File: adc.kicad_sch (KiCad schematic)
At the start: 45 parts, among them J10 Conn_01x02_Pin, J11 Conn_01x02_Pin, J12 Conn_01x02_Pin, J14 Conn_01x02_Pin, J4 Conn_01x03_Pin, J5 Conn_01x03_Pin, J8 Conn_01x03_Pin, J9 Conn_01x03_Pin, U9 LTC2299xUP

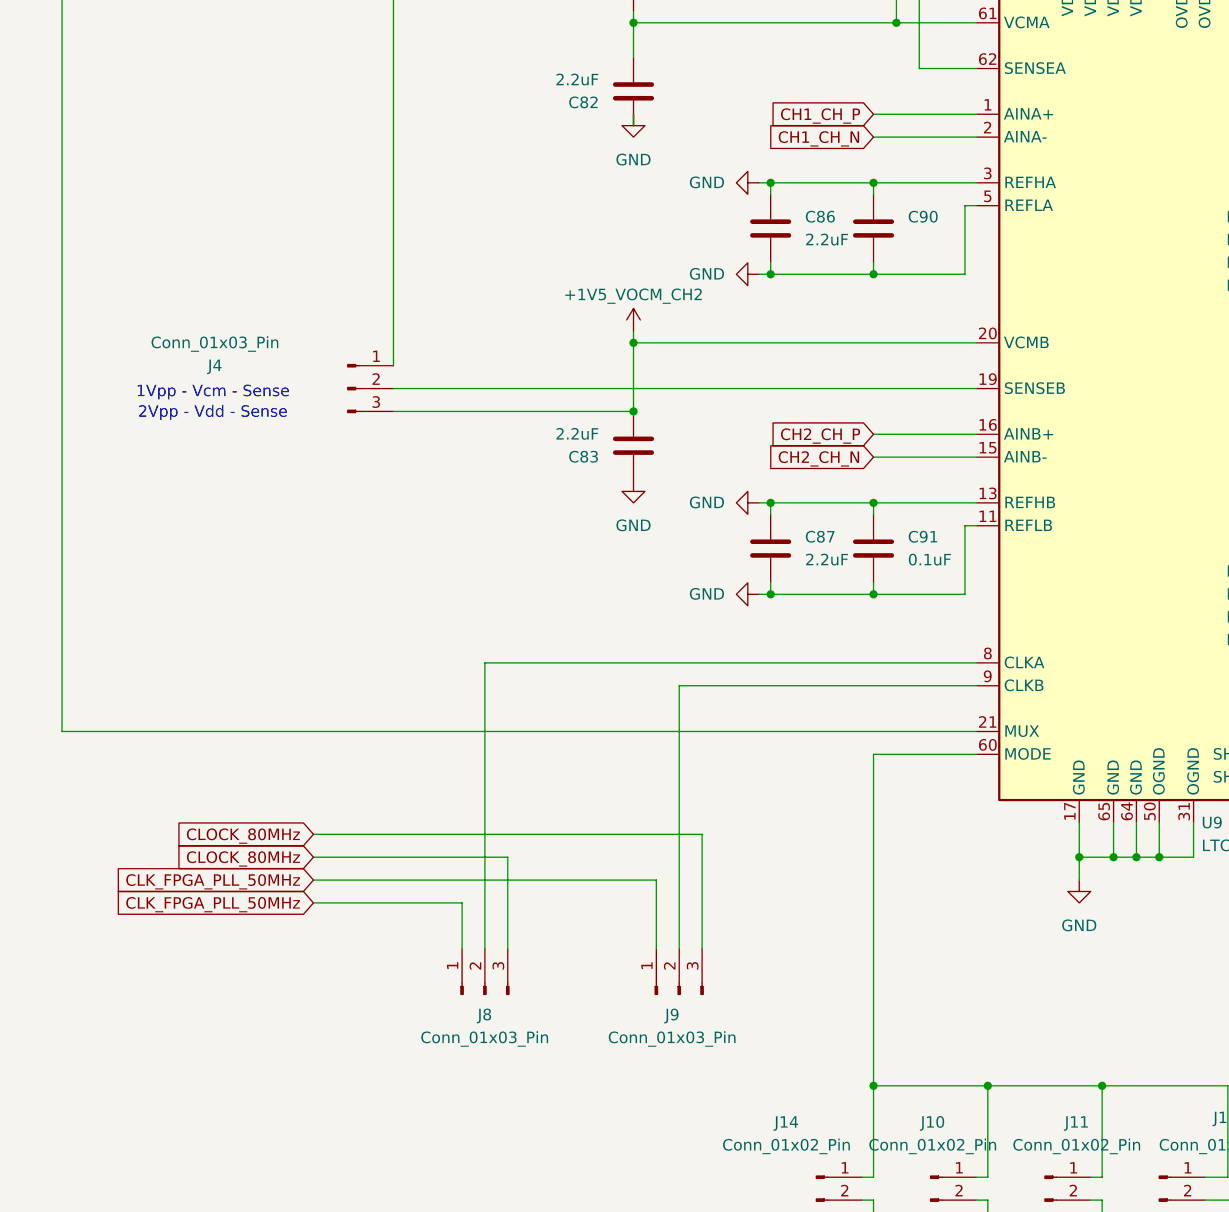
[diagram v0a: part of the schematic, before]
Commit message: Add LDO's
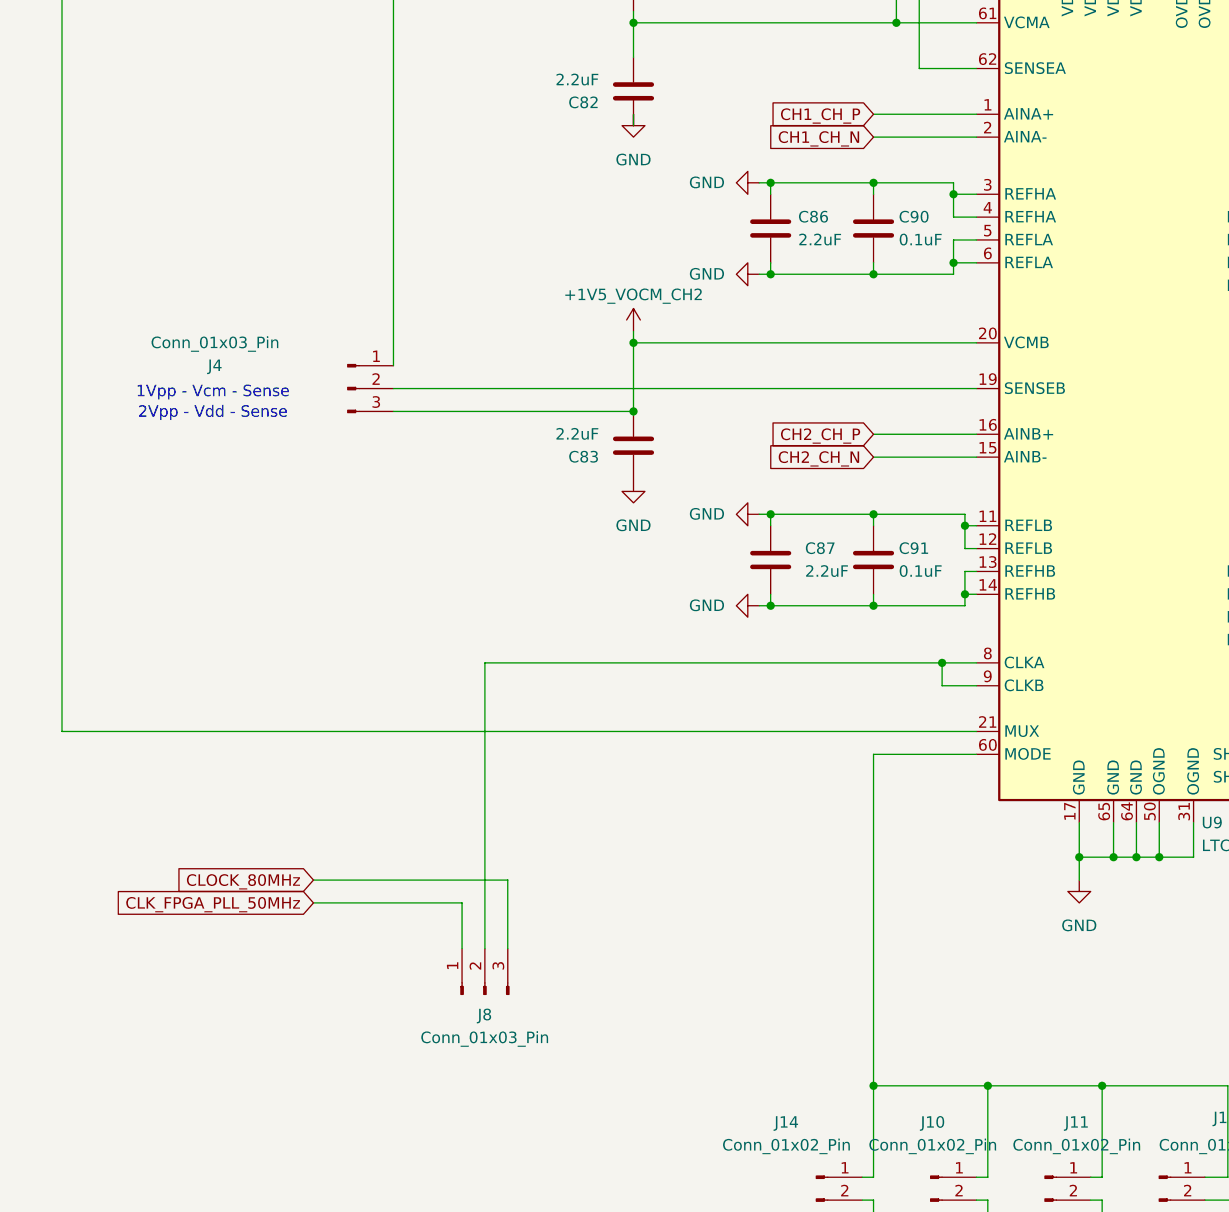
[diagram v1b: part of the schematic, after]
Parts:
- removed J9: Conn_01x03_Pin, Connector_PinHeader_2.54mm:PinHeader_1x03_P2.54mm_Vertical, symbol Connector:Conn_01x03_Pin
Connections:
- net at J8.2 (Pin_2), U9.8 (CLKA): now also U9.9 (CLKB)
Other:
- moved on the sheet: C87, C91

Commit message: Do most of the PCB
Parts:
- J4, J5: footprint TerminalBlock:TerminalBlock_MaiXu_MX126-5.0-03P_1x03_P5.00mm -> Connector_PinHeader_2.54mm:PinHeader_1x03_P2.54mm_Vertical
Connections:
- net GND: now also R68.2, R70.2
- net at R69.2, R70.1: now also J10.2 (Pin_2)
- net at J11.2 (Pin_2): now also R67.2, R68.1; no longer R68.2
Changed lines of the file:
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@@
 	)
 	(junction
+		(at 266.7 245.11)
+		(diameter 0)
+		(color 0 0 0 0)
+	)
+	(junction
 		(at 203.2 256.54)
 		(diameter 0)
@@
 	)
 	(junction
+		(at 279.4 245.11)
+		(diameter 0)
+		(color 0 0 0 0)
+	)
+	(junction
 		(at 232.41 231.14)
 		(diameter 0)
@@
 	(wire
 		(pts
-			(xy 266.7 243.84) (xy 266.7 247.65)
+			(xy 266.7 243.84) (xy 266.7 245.11)
 		)
 		(stroke
@@
 		)
 	)
+	(wire
+		(pts
+			(xy 274.32 276.86) (xy 274.32 245.11)
+		)
+		(stroke
+			(width 0)
+			(type default)
+		)
+	)
 	(bus
 		(pts
@@
 	(wire
 		(pts
+			(xy 279.4 255.27) (xy 279.4 257.81)
+		)
+		(stroke
+			(width 0)
+			(type default)
+		)
+	)
+	(wire
+		(pts
 			(xy 173.99 86.36) (xy 173.99 83.82)
 		)
@@
 		)
 	)
+	(wire
+		(pts
+			(xy 257.81 245.11) (xy 266.7 245.11)
+		)
+		(stroke
+			(width 0)
+			(type default)
+		)
+	)
 	(bus
 		(pts
@@
 	(wire
 		(pts
+			(xy 279.4 245.11) (xy 279.4 247.65)
+		)
+		(stroke
+			(width 0)
+			(type default)
+		)
+	)
+	(wire
+		(pts
 			(xy 191.77 166.37) (xy 190.5 166.37)
 		)
@@
 	(wire
 		(pts
+			(xy 266.7 257.81) (xy 266.7 255.27)
+		)
+		(stroke
+			(width 0)
+			(type default)
+		)
+	)
+	(wire
+		(pts
 			(xy 132.08 57.15) (xy 139.7 57.15)
 		)
@@
 	(wire
 		(pts
+			(xy 266.7 245.11) (xy 266.7 247.65)
+		)
+		(stroke
+			(width 0)
+			(type default)
+		)
+	)
+	(wire
+		(pts
 			(xy 203.2 156.21) (xy 203.2 157.48)
 		)
@@
 	(wire
 		(pts
+			(xy 274.32 245.11) (xy 279.4 245.11)
+		)
+		(stroke
+			(width 0)
+			(type default)
+		)
+	)
+	(wire
+		(pts
 			(xy 215.9 276.86) (xy 215.9 269.24)
 		)
@@
 	(wire
 		(pts
+			(xy 257.81 273.05) (xy 257.81 245.11)
+		)
+		(stroke
+			(width 0)
+			(type default)
+		)
+	)
+	(wire
+		(pts
 			(xy 212.09 160.02) (xy 212.09 157.48)
 		)
@@
 	(wire
 		(pts
-			(xy 266.7 273.05) (xy 228.6 273.05)
-		)
-		(stroke
-			(width 0)
-			(type default)
-		)
-	)
-	(wire
-		(pts
 			(xy 185.42 93.98) (xy 185.42 97.79)
 		)
@@
 	(wire
 		(pts
-			(xy 266.7 255.27) (xy 266.7 273.05)
-		)
-		(stroke
-			(width 0)
-			(type default)
-		)
-	)
-	(wire
-		(pts
 			(xy 176.53 173.99) (xy 176.53 172.72)
 		)
@@
 	(wire
 		(pts
-			(xy 279.4 243.84) (xy 279.4 247.65)
+			(xy 279.4 243.84) (xy 279.4 245.11)
 		)
 		(stroke
@@
 	(wire
 		(pts
-			(xy 279.4 255.27) (xy 279.4 276.86)
-		)
-		(stroke
-			(width 0)
-			(type default)
-		)
-	)
-	(wire
-		(pts
 			(xy 203.2 186.69) (xy 214.63 186.69)
 		)
@@
 	(wire
 		(pts
-			(xy 279.4 276.86) (xy 215.9 276.86)
+			(xy 271.78 57.15) (xy 279.4 57.15)
 		)
 		(stroke
@@
 	(wire
 		(pts
-			(xy 271.78 57.15) (xy 279.4 57.15)
+			(xy 224.79 106.68) (xy 224.79 128.27)
 		)
 		(stroke
@@
 	(wire
 		(pts
-			(xy 224.79 106.68) (xy 224.79 128.27)
+			(xy 173.99 59.69) (xy 173.99 57.15)
 		)
 		(stroke
@@
 		)
 	)
-	(wire
+	(bus
 		(pts
-			(xy 173.99 59.69) (xy 173.99 57.15)
+			(xy 280.67 181.61) (xy 280.67 184.15)
 		)
 		(stroke
@@
 		)
 	)
-	(bus
+	(wire
 		(pts
-			(xy 280.67 181.61) (xy 280.67 184.15)
+			(xy 228.6 273.05) (xy 257.81 273.05)
 		)
 		(stroke
@@
 	(wire
 		(pts
+			(xy 215.9 276.86) (xy 274.32 276.86)
+		)
+		(stroke
+			(width 0)
+			(type default)
+		)
+	)
+	(wire
+		(pts
 			(xy 229.87 130.81) (xy 229.87 128.27)
 		)
@@
 			)
 		)
-		(property "Footprint" "TerminalBlock:TerminalBlock_MaiXu_MX126-5.0-03P_1x03_P5.00mm"
+		(property "Footprint" "Connector_PinHeader_2.54mm:PinHeader_1x03_P2.54mm_Vertical"
 			(at 208.28 123.19 0)
 			(effects
@@
 	)
 	(symbol
+		(lib_id "power:GND")
+		(at 266.7 257.81 0)
+		(unit 1)
+		(exclude_from_sim no)
+		(in_bom yes)
+		(on_board yes)
+		(dnp no)
+		(fields_autoplaced yes)
+		(property "Reference" "#PWR0275"
+			(at 266.7 264.16 0)
+			(effects
+				(font
+					(size 1.27 1.27)
+				)
+				(hide yes)
+			)
+		)
+		(property "Value" "GND"
+			(at 266.7 262.89 0)
+			(effects
+				(font
+					(size 1.27 1.27)
+				)
+			)
+		)
+		(property "Footprint" ""
+			(at 266.7 257.81 0)
+			(effects
+				(font
+					(size 1.27 1.27)
+				)
+				(hide yes)
+			)
+		)
+		(property "Datasheet" ""
+			(at 266.7 257.81 0)
+			(effects
+				(font
+					(size 1.27 1.27)
+				)
+				(hide yes)
+			)
+		)
+		(property "Description" "Power symbol creates a global label with name \"GND\" , ground"
+			(at 266.7 257.81 0)
+			(effects
+				(font
+					(size 1.27 1.27)
+				)
+				(hide yes)
+			)
+		)
+		(pin "1"
+		)
+		(instances
+			(project "DigitalOsciloscope"
+				(path "/553deb7b-4100-40fe-99d2-0c7b4b56aad2/800cc051-5da0-4b0f-90b7-cfba3f489ea8"
+					(reference "#PWR0275")
+					(unit 1)
+				)
+			)
+		)
+	)
+	(symbol
 		(lib_id "Connector:Conn_01x02_Pin")
 		(at 209.55 266.7 0)
@@
 			)
 		)
-		(property "Footprint" "TerminalBlock:TerminalBlock_MaiXu_MX126-5.0-03P_1x03_P5.00mm"
+		(property "Footprint" "Connector_PinHeader_2.54mm:PinHeader_1x03_P2.54mm_Vertical"
 			(at 144.78 179.07 0)
 			(effects
@@
 					(unit 1)
 				)
+			)
+		)
+	)
+	(symbol
+		(lib_id "power:GND")
+		(at 279.4 257.81 0)
+		(unit 1)
+		(exclude_from_sim no)
+		(in_bom yes)
+		(on_board yes)
+		(dnp no)
+		(fields_autoplaced yes)
+		(property "Reference" "#PWR0278"
+			(at 279.4 264.16 0)
+			(effects
+				(font
+					(size 1.27 1.27)
+				)
+				(hide yes)
+			)
+		)
+		(property "Value" "GND"
+			(at 279.4 262.89 0)
+			(effects
+				(font
+					(size 1.27 1.27)
+				)
+			)
+		)
+		(property "Footprint" ""
+			(at 279.4 257.81 0)
+			(effects
+				(font
+					(size 1.27 1.27)
+				)
+				(hide yes)
+			)
+		)
+		(property "Datasheet" ""
+			(at 279.4 257.81 0)
+			(effects
+				(font
+					(size 1.27 1.27)
+				)
+				(hide yes)
+			)
+		)
+		(property "Description" "Power symbol creates a global label with name \"GND\" , ground"
+			(at 279.4 257.81 0)
+			(effects
+				(font
+					(size 1.27 1.27)
+				)
+				(hide yes)
+			)
+		)
+		(pin "1"
+		)
+		(instances
+			(project "DigitalOsciloscope"
+				(path "/553deb7b-4100-40fe-99d2-0c7b4b56aad2/800cc051-5da0-4b0f-90b7-cfba3f489ea8"
+					(reference "#PWR0278")
+					(unit 1)
+				)

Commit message: Place all componenets
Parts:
- renumbered C98 to C100, C99 to C101, C76 to C78, C77 to C79, C78 to C80, C79 to C81, C80 to C82, C81 to C83, C82 to C84, C83 to C85, C84 to C86, C85 to C87, C86 to C88, C87 to C89, C88 to C90, C89 to C91, C90 to C92, C91 to C93, C92 to C94, C93 to C95, C94 to C96, C95 to C97, C96 to C98, C97 to C99, J12 to J10, J8 to J5, J14 to J6, J5 to J7, J10 to J8, J11 to J9, R67 to R54, R68 to R55, R69 to R56, R70 to R57

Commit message: Finish channel 1 rework
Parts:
- renumbered C101 to C100, C78 to C77, C79 to C78, C80 to C79, C81 to C80, C82 to C81, C83 to C82, C84 to C83, C85 to C84, C86 to C85, C87 to C86, C88 to C87, C89 to C88, C90 to C89, C91 to C90, C92 to C91, C93 to C92, C94 to C93, C95 to C94, C96 to C95, C97 to C96, C98 to C97, C99 to C98, C100 to C99

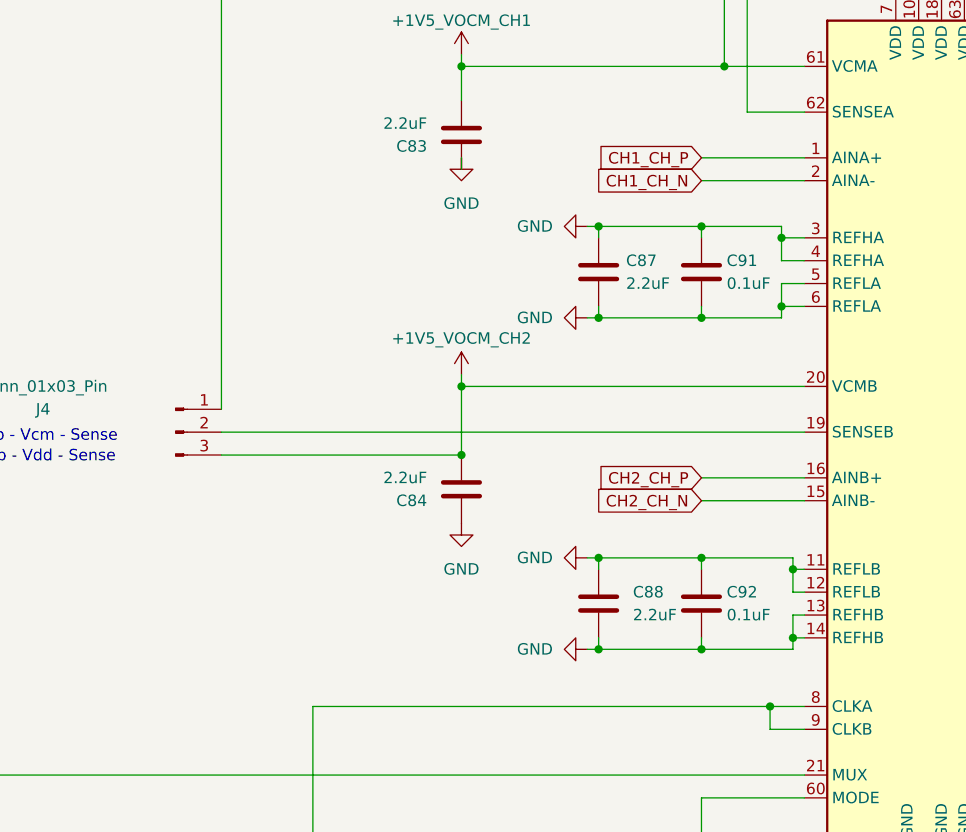
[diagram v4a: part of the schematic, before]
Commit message: Fix bug in adc ref voltage
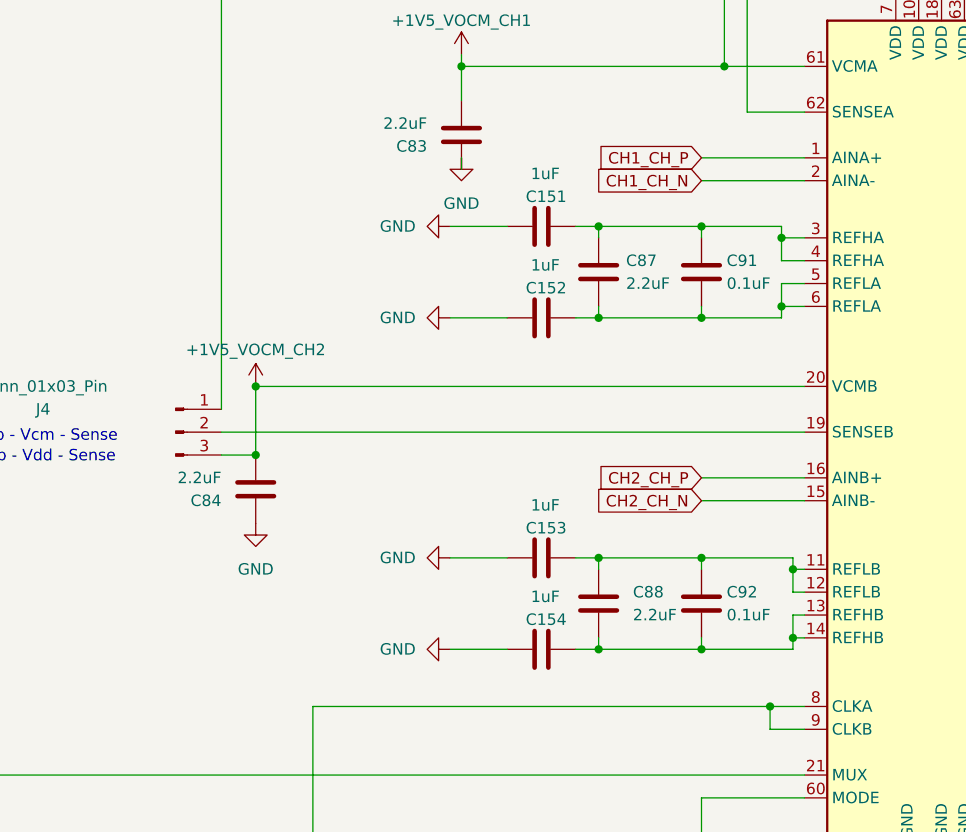
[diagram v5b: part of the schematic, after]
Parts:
- added C151, C152, C153, C154: 1uF, Capacitor_SMD:C_0805_2012Metric, symbol Device:C
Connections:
- net GND: now also C151.1, C152.1, C153.1, C154.1; no longer C87.1, C87.2, C88.1, C88.2, C91.1, C91.2, C92.1, C92.2, U9.11 (REFLB), U9.12 (REFLB), U9.13 (REFHB), U9.14 (REFHB), U9.3 (REFHA), U9.4 (REFHA), U9.5 (REFLA), U9.6 (REFLA)
- new net: C151.2, C87.1, C91.1, U9.3 (REFHA), U9.4 (REFHA)
- new net: C152.2, C87.2, C91.2, U9.5 (REFLA), U9.6 (REFLA)
- new net: C153.2, C88.1, C92.1, U9.11 (REFLB), U9.12 (REFLB)
- new net: C154.2, C88.2, C92.2, U9.13 (REFHB), U9.14 (REFHB)
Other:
- moved on the sheet: C84

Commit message: Changes after major PCB review
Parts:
- J10, J6, J8, J9: footprint Connector_PinHeader_2.54mm:PinHeader_1x02_P2.54mm_Vertical -> Connector_PinHeader_2.54mm:PinHeader_1x02_P2.54mm_Horizontal
- J4, J5, J7: footprint Connector_PinHeader_2.54mm:PinHeader_1x03_P2.54mm_Vertical -> Connector_PinHeader_2.54mm:PinHeader_1x03_P2.54mm_Horizontal
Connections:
- net CLK_FPGA_PLL_50MHz: now also J5.3 (Pin_3); no longer J5.1 (Pin_1)
- net CLOCK_80MHz: now also J5.1 (Pin_1); no longer J5.3 (Pin_3)
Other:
- moved on the sheet: J5
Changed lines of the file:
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@@
 			)
 		)
-		(property "Footprint" "Connector_PinHeader_2.54mm:PinHeader_1x03_P2.54mm_Vertical"
+		(property "Footprint" "Connector_PinHeader_2.54mm:PinHeader_1x03_P2.54mm_Horizontal"
 			(at 208.28 123.19 0)
 			(effects
@@
 			)
 		)
-		(property "Footprint" "Connector_PinHeader_2.54mm:PinHeader_1x02_P2.54mm_Vertical"
+		(property "Footprint" "Connector_PinHeader_2.54mm:PinHeader_1x02_P2.54mm_Horizontal"
 			(at 196.85 266.7 0)
 			(effects
@@
 			)
 		)
-		(property "Footprint" "Connector_PinHeader_2.54mm:PinHeader_1x02_P2.54mm_Vertical"
+		(property "Footprint" "Connector_PinHeader_2.54mm:PinHeader_1x02_P2.54mm_Horizontal"
 			(at 209.55 266.7 0)
 			(effects
@@
 	(symbol
 		(lib_id "Connector:Conn_01x03_Pin")
-		(at 160.02 246.38 90)
+		(at 160.02 246.38 270)
+		(mirror x)
 		(unit 1)
 		(exclude_from_sim no)
@@
 			)
 		)
-		(property "Footprint" "Connector_PinHeader_2.54mm:PinHeader_1x03_P2.54mm_Vertical"
+		(property "Footprint" "Connector_PinHeader_2.54mm:PinHeader_1x03_P2.54mm_Horizontal"
 			(at 160.02 246.38 0)
 			(effects
@@
 			)
 		)
-		(property "Footprint" "Connector_PinHeader_2.54mm:PinHeader_1x02_P2.54mm_Vertical"
+		(property "Footprint" "Connector_PinHeader_2.54mm:PinHeader_1x02_P2.54mm_Horizontal"
 			(at 222.25 266.7 0)
 			(effects
@@
 			)
 		)
-		(property "Footprint" "Connector_PinHeader_2.54mm:PinHeader_1x02_P2.54mm_Vertical"
+		(property "Footprint" "Connector_PinHeader_2.54mm:PinHeader_1x02_P2.54mm_Horizontal"
 			(at 234.95 266.7 0)
 			(effects
@@
 			)
 		)
-		(property "Footprint" "Connector_PinHeader_2.54mm:PinHeader_1x03_P2.54mm_Vertical"
+		(property "Footprint" "Connector_PinHeader_2.54mm:PinHeader_1x03_P2.54mm_Horizontal"
 			(at 144.78 179.07 0)
 			(effects
